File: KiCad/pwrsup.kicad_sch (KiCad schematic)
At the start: 16 parts, among them U1 L7805, U2 LT1054CS8#TRPBF, U3 MCP6002-xP

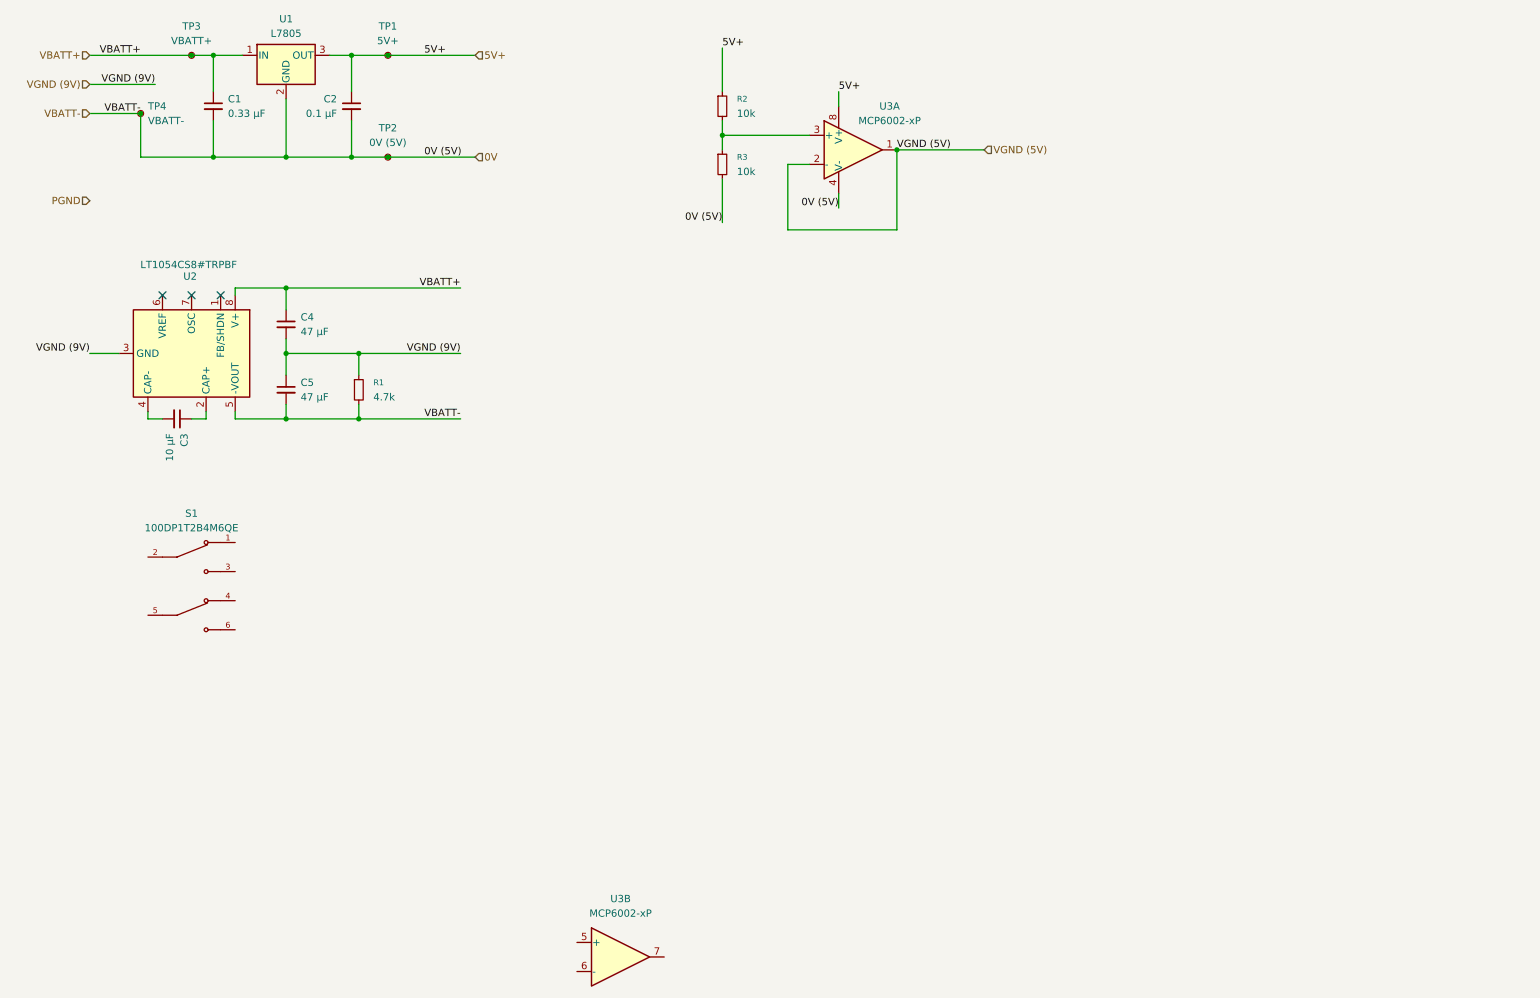
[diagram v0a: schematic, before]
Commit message: Finish power supply, make waveform generator.
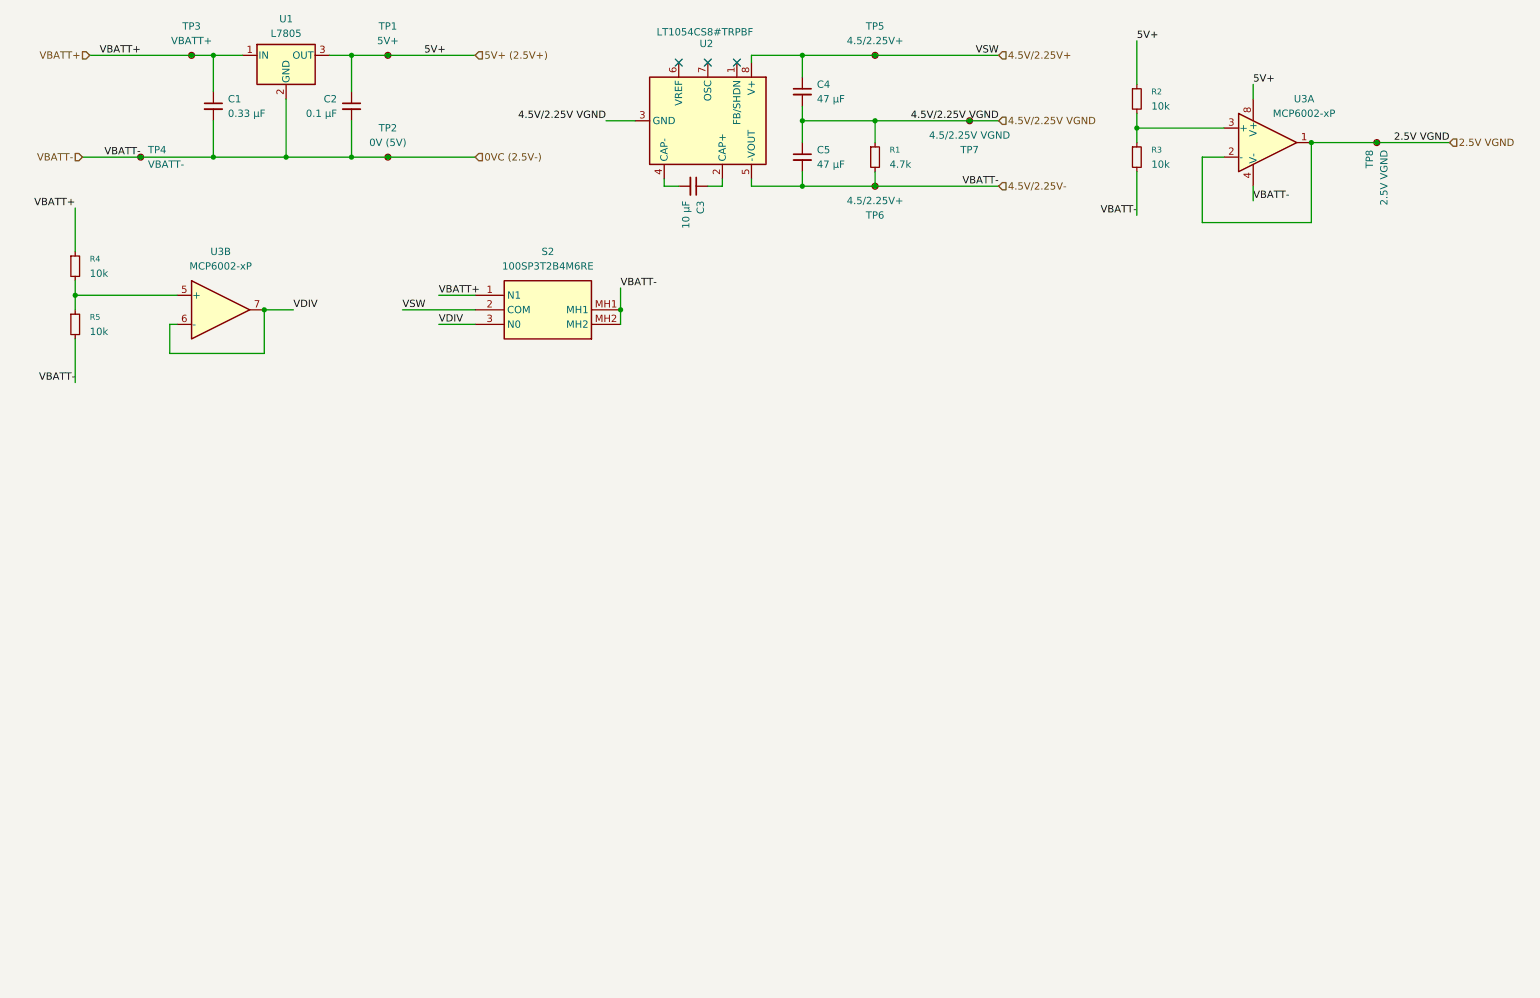
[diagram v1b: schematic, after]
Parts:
- removed S1: 100DP1T2B4M6QE, 100DP1T2B4M6QE:SW_100DP1T2B4M6QE, symbol 100DP1T2B4M6QE:100DP1T2B4M6QE
- added R4, R5: 10k, symbol Device:R_Small
- added S2: 100SP3T2B4M6RE, 100SP3T2B4M6RE, symbol 100SP3T2B4M6RE:100SP3T2B4M6RE
- added TP5, TP6: 4.5/2.25V+, symbol Connector:TestPoint_Small
- added TP7: 4.5/2.25V VGND, symbol Connector:TestPoint_Small
- added TP8: 2.5V VGND, symbol Connector:TestPoint_Small
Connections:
- net VBATT+: now also R4.1, S2.1 (N1); no longer C4.1, U2.8 (V+)
- net at U3.5 (+): now also R4.2, R5.1
- net VDIV: now reaches U3.6 (-)
- net VDIV: now also U3.7, S2.3 (N0)
- net 0V renamed 0VC (2.5V-)
- net 0VC (2.5V-): now also R5.2, S2.MH1, S2.MH2, TP6.1
- net 5V+ renamed 5V+ (2.5V+)
- net VGND (5V) renamed 2.5V VGND
- net 2.5V VGND: now also TP8.1
- net VGND (9V) renamed 4.5V/2.25V VGND
- net 4.5V/2.25V VGND: now also TP7.1
- new net 4.5V/2.25V+: C4.1, S2.2 (COM), TP5.1, U2.8 (V+)
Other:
- moved on the sheet: C3, C4, C5, R1, R2, R3, TP4, U2, U3A, U3B

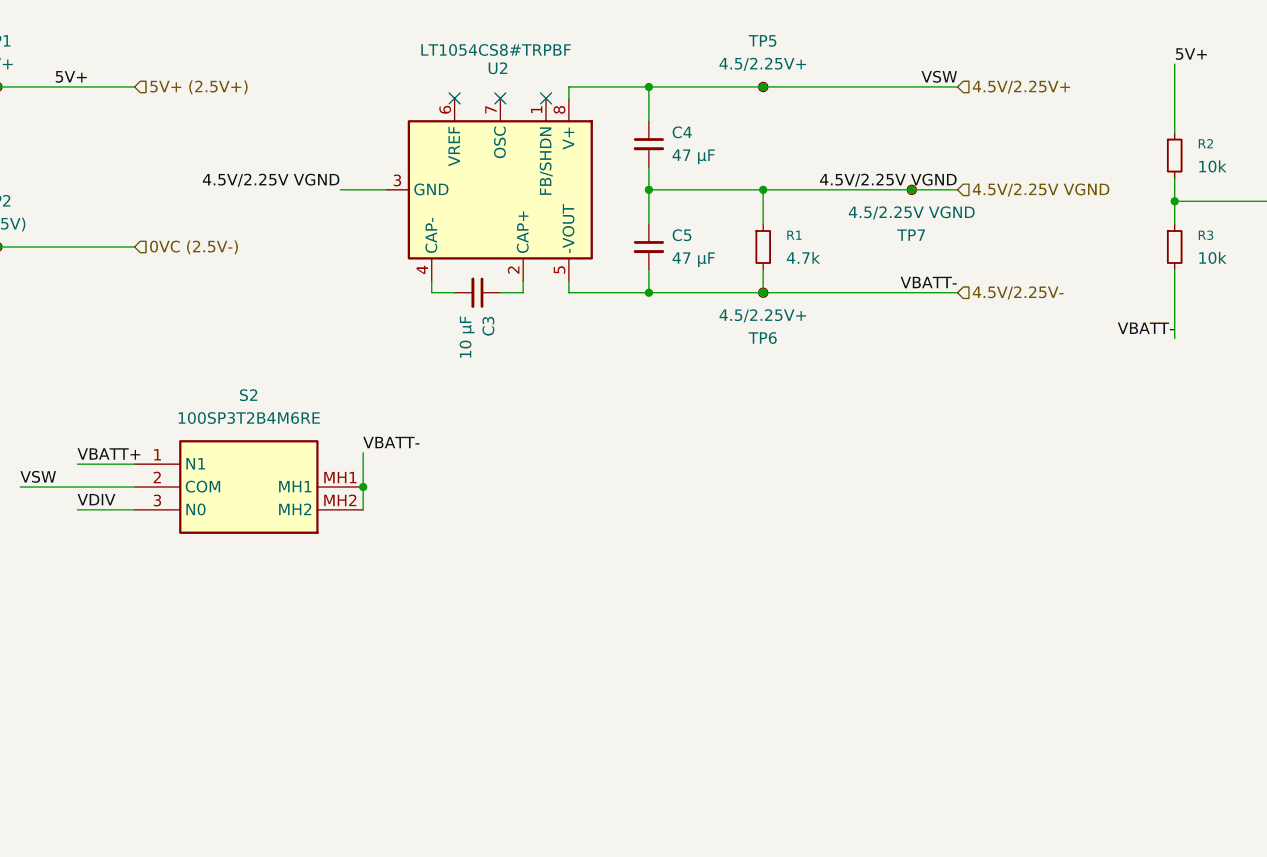
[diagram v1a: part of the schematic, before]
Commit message: Change to TI rail splitter.
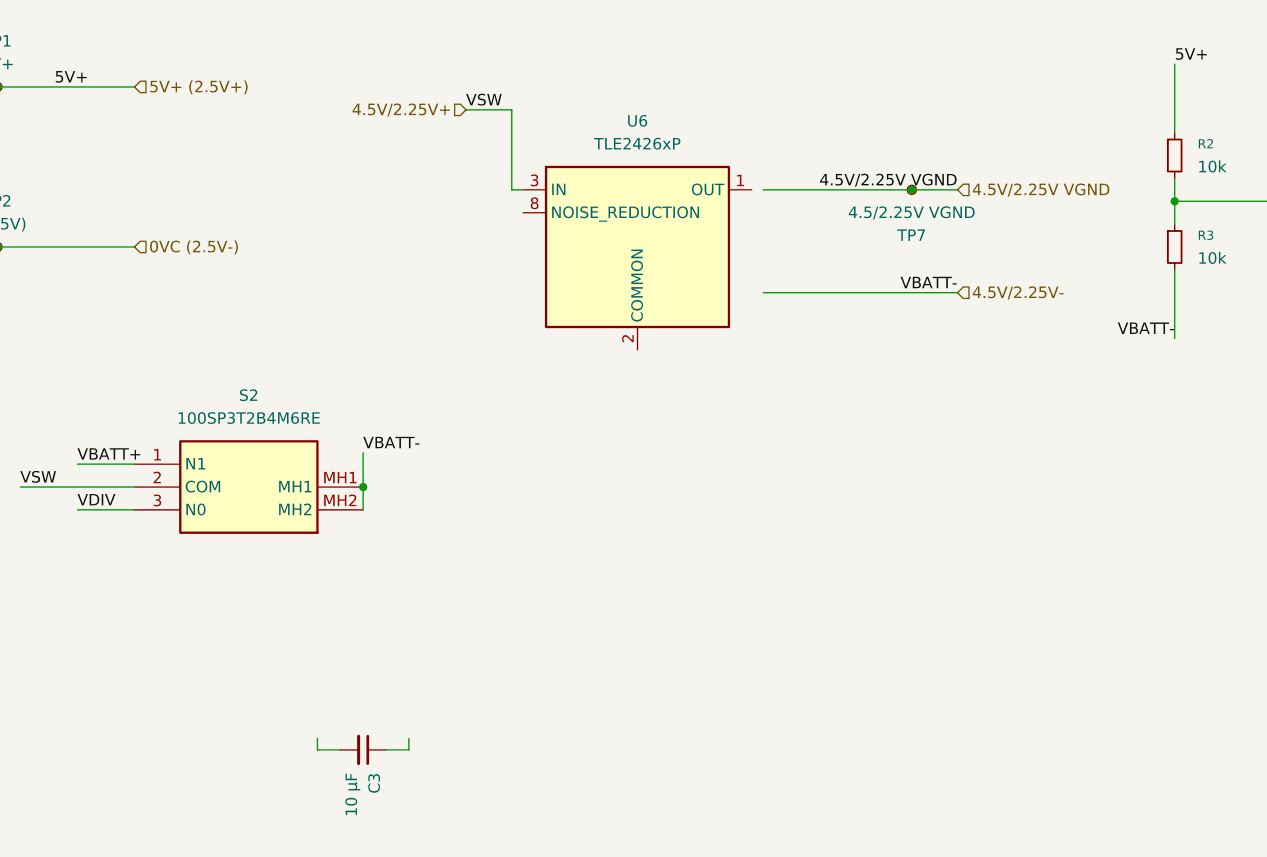
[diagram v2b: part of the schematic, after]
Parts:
- removed C4, C5: 47 µF, symbol Device:C_Small
- removed R1: 4.7k, symbol Device:R_Small
- removed TP5, TP6: 4.5/2.25V+, symbol Connector:TestPoint_Small
- removed U2: LT1054CS8#TRPBF, Package_SO:SOIC-8_3.9x4.9mm_P1.27mm, symbol Regulator_SwitchedCapacitor:LT1054
- added U6: TLE2426xP, Package_DIP:DIP-8_W7.62mm, symbol Reference_Voltage:TLE2426xP
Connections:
- net 4.5V/2.25V+: now also U6.3 (IN)
- no-connect marks 3 -> 0
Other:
- moved on the sheet: C3

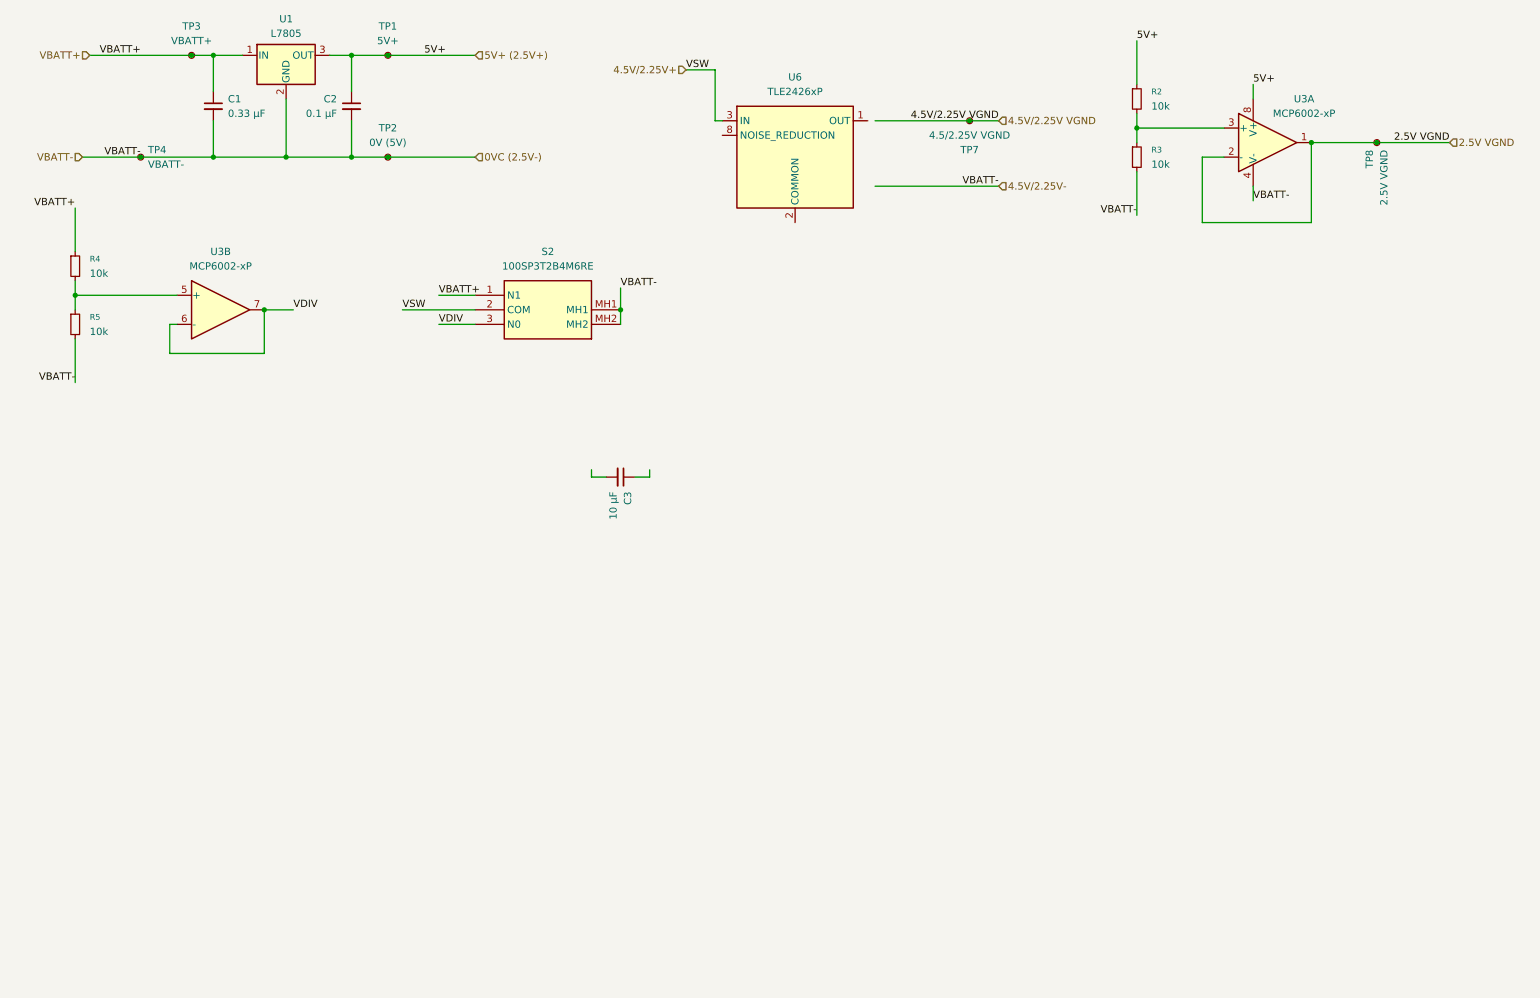
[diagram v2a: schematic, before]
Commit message: Swapped mcp6002 rail splitter for TI TLE2426xP
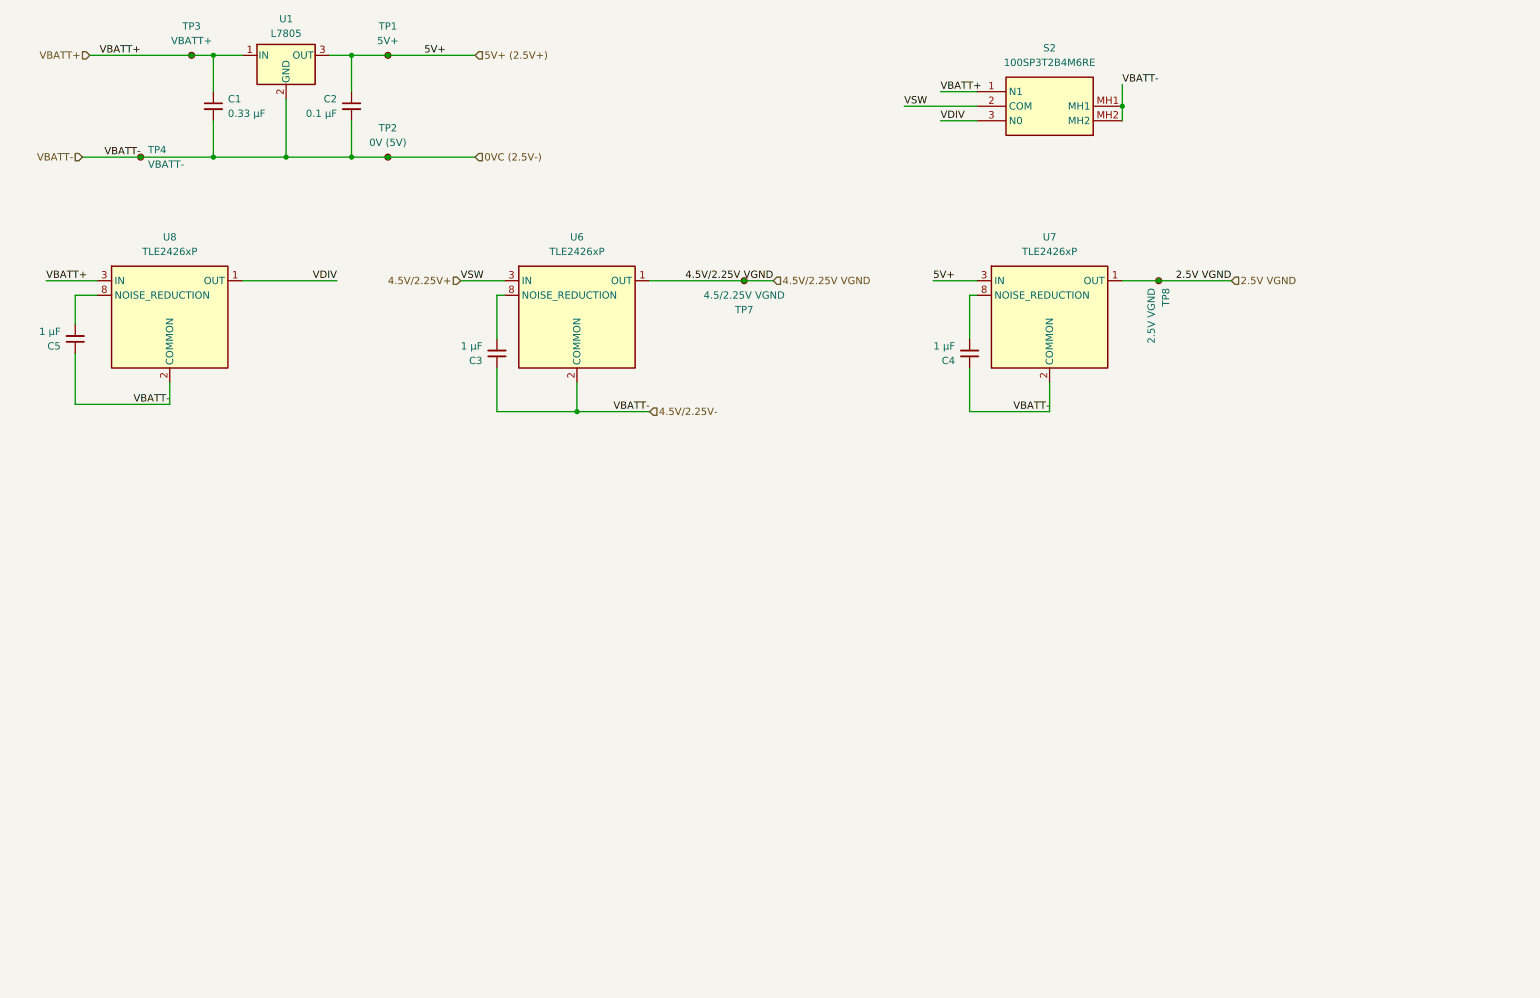
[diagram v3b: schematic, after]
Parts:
- removed R2, R3, R4, R5: 10k, symbol Device:R_Small
- removed U3: MCP6002-xP, Package_SO:SOIC-8_3.9x4.9mm_P1.27mm, symbol Amplifier_Operational:MCP6002-xP
- added C4, C5: 1 µF, symbol Device:C_Small
- added U7, U8: TLE2426xP, Package_DIP:DIP-8_W7.62mm, symbol Reference_Voltage:TLE2426xP
- C3: value 10 µF -> 1 µF
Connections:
- net 0VC (2.5V-): now also C3.1, U6.2 (COMMON), C4.1, C5.1, U7.2 (COMMON), U8.2 (COMMON)
- net 2.5V VGND: now also U7.1 (OUT)
- net 4.5V/2.25V VGND: now also U6.1 (OUT)
- net 5V+ (2.5V+): now also U7.3 (IN)
- net VBATT+: now also U8.3 (IN)
- net VDIV: now also U8.1 (OUT)
- net at C3.2: now also U6.8 (NOISE_REDUCTION)
- new net: C4.2, U7.8 (NOISE_REDUCTION)
- new net: C5.2, U8.8 (NOISE_REDUCTION)
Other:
- moved on the sheet: C3, S2, TP7, TP8, U6

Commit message: started edited pcb layout
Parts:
- S2: footprint 100SP3T2B4M6RE -> 100SP3T2B4M6RE:100SP3T2B4M6RE
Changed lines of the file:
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@@
 			)
 		)
-		(property "Footprint" "100SP3T2B4M6RE"
-			(at 193.04 -61.9 0)
+		(property "Footprint" "100SP3T2B4M6RE:100SP3T2B4M6RE"
+			(at 105.41 -26.34 0)
 			(effects
 				(font

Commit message: added footprints to schematic
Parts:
- C1, C2: footprint (none) -> Capacitor_SMD:C_0201_0603Metric
- U1: footprint (none) -> Package_TO_SOT_THT:TO-218-3_Vertical
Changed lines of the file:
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@@
 			)
 		)
-		(property "Footprint" ""
+		(property "Footprint" "Package_TO_SOT_THT:TO-218-3_Vertical"
 			(at 69.215 25.4 0)
 			(effects
@@
 			)
 		)
-		(property "Footprint" ""
+		(property "Footprint" "Capacitor_SMD:C_0201_0603Metric"
 			(at 80.01 30.48 0)
 			(effects
@@
 			)
 		)
-		(property "Footprint" ""
+		(property "Footprint" "Capacitor_SMD:C_0201_0603Metric"
 			(at 55.88 30.48 0)
 			(effects

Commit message: Add power led
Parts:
- C1, C2: footprint Capacitor_SMD:C_0201_0603Metric -> (none)
- U1: footprint Package_TO_SOT_THT:TO-218-3_Vertical -> (none)
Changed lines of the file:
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@@
 			)
 		)
-		(property "Footprint" "Package_TO_SOT_THT:TO-218-3_Vertical"
+		(property "Footprint" ""
 			(at 69.215 25.4 0)
 			(effects
@@
 			)
 		)
-		(property "Footprint" "Capacitor_SMD:C_0201_0603Metric"
+		(property "Footprint" ""
 			(at 80.01 30.48 0)
 			(effects
@@
 			)
 		)
-		(property "Footprint" "Capacitor_SMD:C_0201_0603Metric"
+		(property "Footprint" ""
 			(at 55.88 30.48 0)
 			(effects

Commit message: updated footprint to be all THT, battery holder still not there
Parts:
- C1, C2: footprint (none) -> Capacitor_THT:C_Disc_D5.0mm_W2.5mm_P2.50mm
- U1: footprint (none) -> Package_TO_SOT_THT:TO-218-3_Vertical
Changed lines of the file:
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@@
 			)
 		)
-		(property "Footprint" ""
+		(property "Footprint" "Package_TO_SOT_THT:TO-218-3_Vertical"
 			(at 69.215 25.4 0)
 			(effects
@@
 			)
 		)
-		(property "Footprint" ""
+		(property "Footprint" "Capacitor_THT:C_Disc_D5.0mm_W2.5mm_P2.50mm"
 			(at 80.01 30.48 0)
 			(effects
@@
 			)
 		)
-		(property "Footprint" ""
+		(property "Footprint" "Capacitor_THT:C_Disc_D5.0mm_W2.5mm_P2.50mm"
 			(at 55.88 30.48 0)
 			(effects
